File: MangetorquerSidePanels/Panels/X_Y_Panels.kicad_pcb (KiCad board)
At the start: 6 copper layers, 82 x 108 mm, 61 parts, among them J6 Through_Hole_1, Q1 BSS138DWQ-7, Q2 MBT2222ADW1T1, Q3 BSS138DWQ-7, Q4 MBT2222ADW1T1, U1 DRV8830DGQ, U2 BD50GC0WEFJ, U3 OPT3001

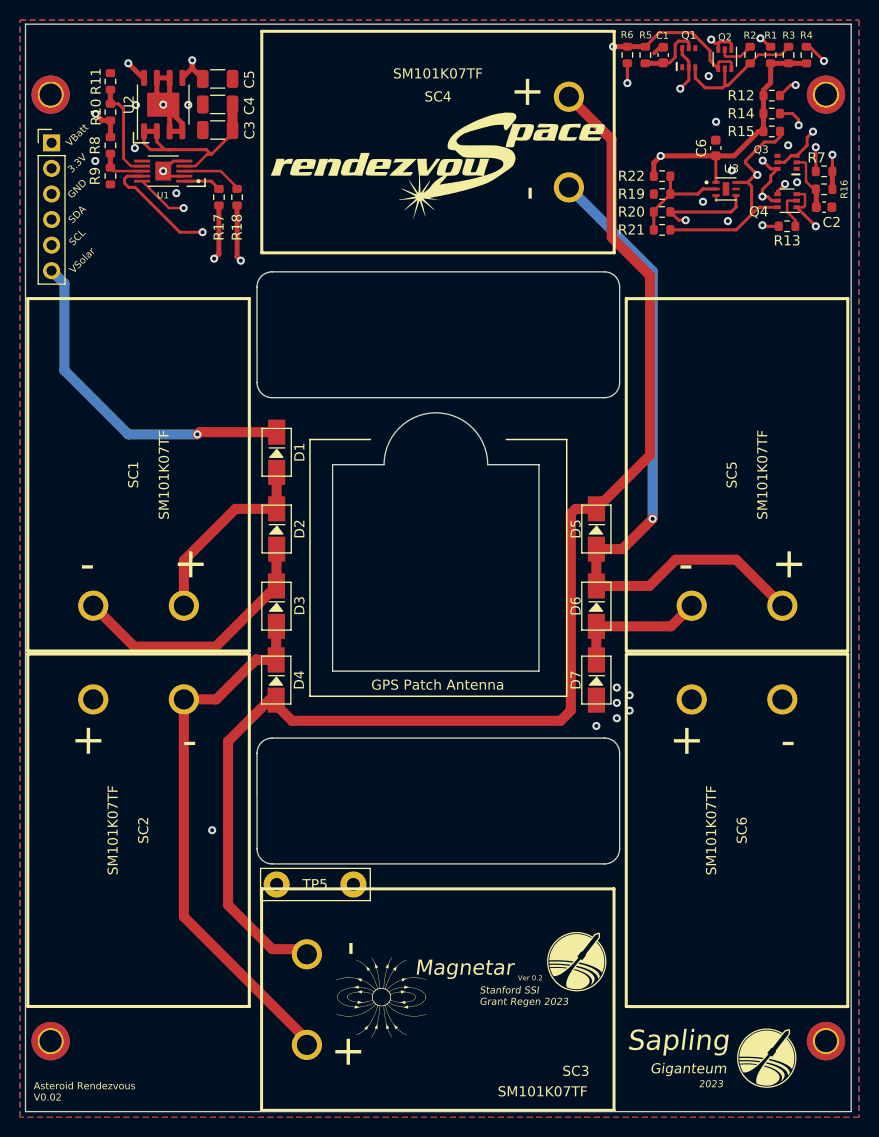
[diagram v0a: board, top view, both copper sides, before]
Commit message: added magnetorquers
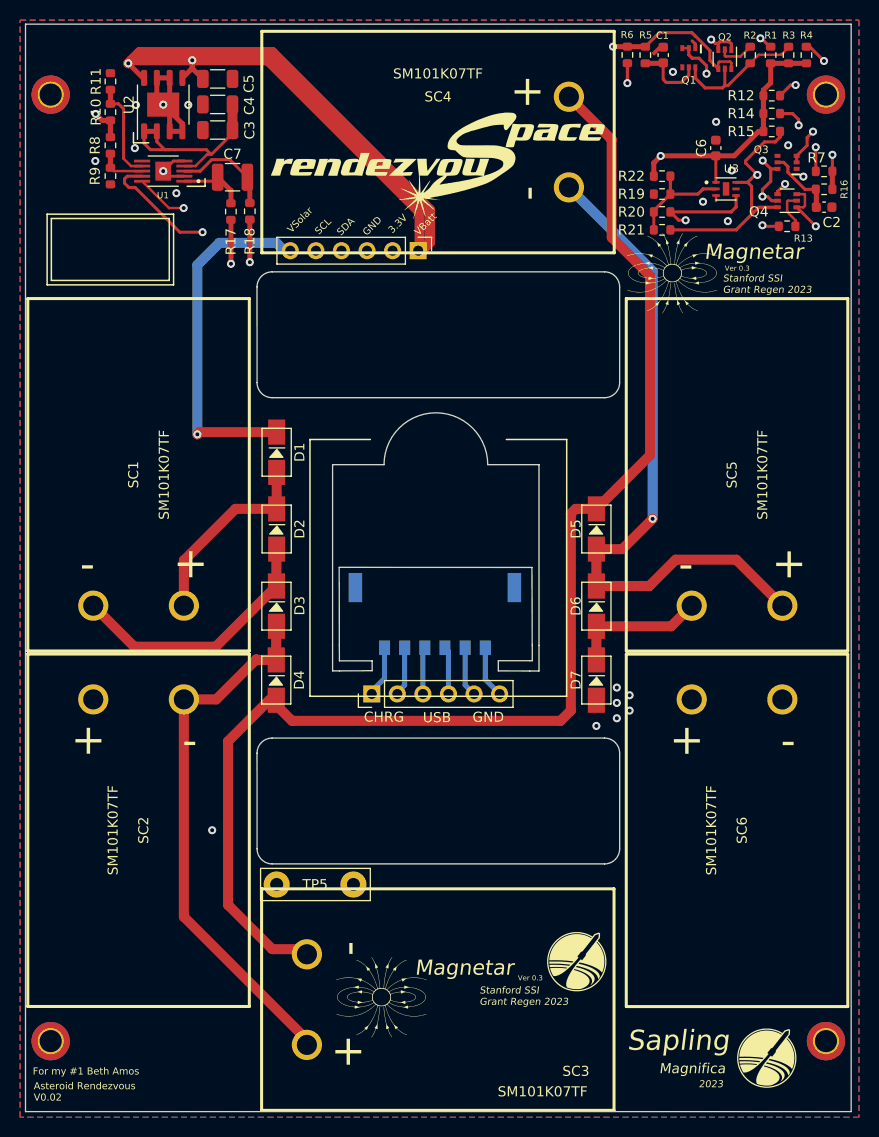
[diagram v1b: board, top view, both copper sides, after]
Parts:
- removed the REF** at (178.1, 121.7)
- added C7: XXuF, Capacitor_SMD:C_1210_3225Metric, F.Cu at (121.9, 53.2)
- added J1: Through_Hole_1, Connector_PinHeader_2.54mm:PinHeader_1x06_P2.54mm_Vertical, F.Cu at (135.7, 104.5)
- added J2: MOLEX_2053380006, panels:MOLEX_2053380006, B.Cu at (141.9, 96.4)
- added REF**: logo_magnet_1, panels:logo_magnet_1, F.Cu at (165.5, 62.7)
- U2: value BD50GC0WEFJ -> BD60GC0WEFJ
- moved J6 37.9 mm to (140.3, 60.5), turned to -90 degrees
- moved R18 1.88 mm to (123.6, 56.6)
- moved R17 1.85 mm to (121.7, 56.6)
- turned Q1 to -90 degrees
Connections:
- Q1 pad 3: Net-(Q1-Pad3) -> Net-(Q1-Pad2)
- Q1 pad 6: Net-(Q1-Pad2) -> Net-(Q1-Pad6)
- Q2 pad 5: Net-(Q1-Pad3) -> Net-(Q1-Pad6)
- Q3 pad 2: Net-(C2-Pad1) -> Net-(Q3-Pad2)
- Q3 pad 3: Net-(Q3-Pad3) -> Net-(Q3-Pad2)
- Q3 pad 5: Net-(Q3-Pad3) -> Net-(C2-Pad1)
- R12 pad 1: Net-(Q3-Pad3) -> Net-(Q3-Pad2)
- R2 pad 1: Net-(Q1-Pad3) -> Net-(Q1-Pad6)
- R3 pad 2: Net-(Q1-Pad3) -> Net-(Q1-Pad6)
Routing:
- net VBATT: track 28.4 -> 96.8 mm
- net +3V3: track 89.9 -> 61.1 mm
- net SDA: track 96.2 -> 68.4 mm
- net SCL: track 79.4 -> 54.0 mm
- net Net-(Q1-Pad6): track 0.00 -> 14.1 mm
- net Net-(Q1-Pad3): track 14.1 -> 0.00 mm
- net Net-(Q3-Pad3): track 12.6 -> 0.00 mm, vias 2 -> 0
- net Net-(Q3-Pad2): track 0.00 -> 11.0 mm, vias 0 -> 2
- net Net-(J1-Pad6): track 0.00 -> 5.18 mm
- net Net-(J1-Pad1): track 0.00 -> 5.12 mm
- net Net-(J1-Pad5): track 0.00 -> 4.96 mm
- net Net-(J1-Pad2): track 0.00 -> 4.89 mm
- net Net-(J1-Pad4): track 0.00 -> 4.73 mm
- net Net-(J1-Pad3): track 0.00 -> 4.67 mm
- net Net-(C7-Pad2): track 6.05 -> 10.1 mm
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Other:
- outline, holes or cut-outs redrawn
- board text added: "CHRG"
- board text added: "For my #1 Beth Amos"
- board text added: "Magnifica"
- board text added: "USB"
- board text added: "Ver 0.3"
- board text removed: "GPS Patch Antenna"
- board text removed: "Giganteum"
- board text removed: "Ver 0.2"
